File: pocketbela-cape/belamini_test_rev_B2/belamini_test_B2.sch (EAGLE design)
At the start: 10 parts, among them J1 M10SILK_FEMALE_PTH, J3 22-23-2031, J4 22-23-2031

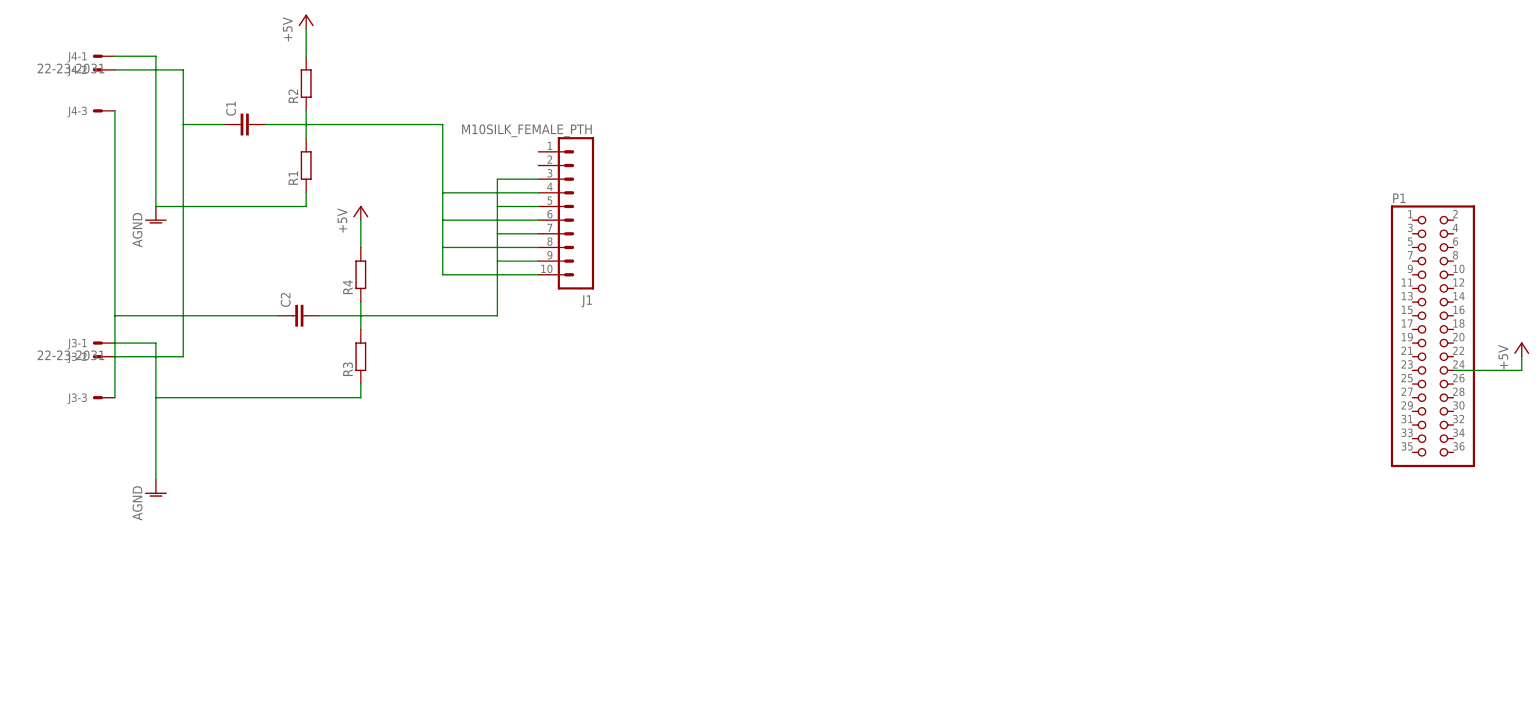
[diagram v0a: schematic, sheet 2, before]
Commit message: belamini test jig attempt 2
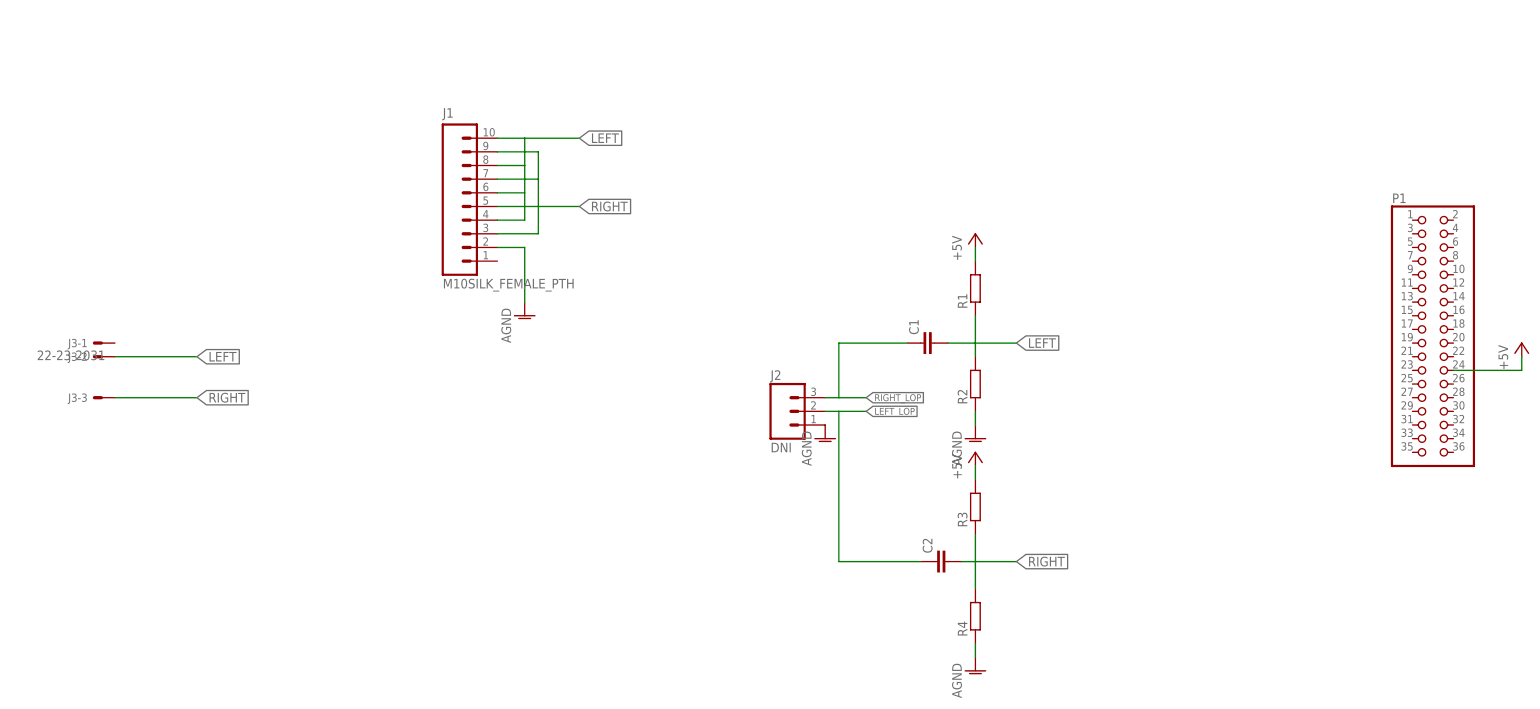
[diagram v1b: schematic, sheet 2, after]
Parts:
- removed J4: 22-23-2031, con-molex:22-23-2031
- added J2: DNI, SparkFun-Connectors:M03PTH
- C1, C2: device resistor:C-EU050-025X075 -> capacitor-wima:C5/2.5
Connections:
- removed net N$1: C2.2, J1.3, J1.5, J1.7, J1.9, R3.2, R4.1
- removed net N$2: C1.2, J1.10, J1.4, J1.6, J1.8, R1.2, R2.1
- removed net N$3: C1.1, J3-2.S, J4-2.S
- removed net N$4: C2.1, J3-3.S, J4-3.S
- new net AGND: J1.2, R2.1, R4.1
- new net LEFT: C1.2, J1.10, J1.4, J1.6, J1.8, J3-2.S, R1.1, R2.2
- new net LEFT_LOP: C2.1, J2.2
- new net RIGHT: C2.2, J1.3, J1.5, J1.7, J1.9, J3-3.S, R3.1, R4.2
- new net RIGHT_LOP: C1.1, J2.3
- net +5V_SYS: now also R1.2, R3.2; no longer R2.2, R4.2
- net GND: now also J2.1; no longer J3-1.S, J4-1.S, R1.1, R3.1
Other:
- moved on the sheet: C1, C2, J1, R1, R2, R3, R4

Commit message: Line out is DC-coupled, so no need for external components
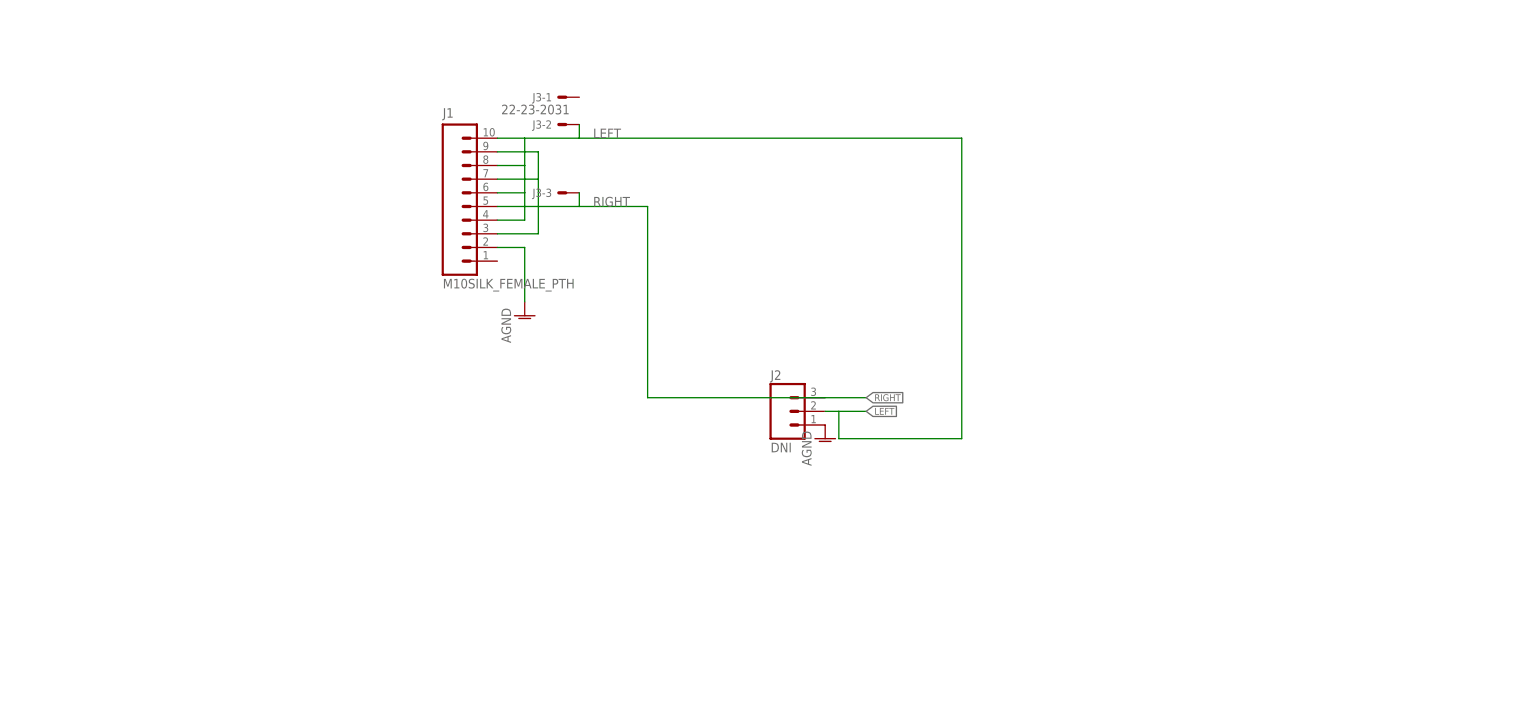
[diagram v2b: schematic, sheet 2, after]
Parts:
- removed C1, C2: (no value), capacitor-wima:C5/2.5
- removed P1: (no value), pinhead:PINHD-2X18
- removed R1, R2, R3, R4: (no value), resistor:R-EU_0204/7
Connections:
- removed net +5V_SYS: P1.24, R1.2, R3.2
- removed net LEFT_LOP: C2.1, J2.2
- removed net RIGHT_LOP: C1.1, J2.3
- net AGND: no longer R2.1, R4.1
- net LEFT: now also J2.2; no longer C1.2, R1.1, R2.2
- net RIGHT: now also J2.3; no longer C2.2, R3.1, R4.2
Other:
- moved on the sheet: J3-1, J3-2, J3-3
